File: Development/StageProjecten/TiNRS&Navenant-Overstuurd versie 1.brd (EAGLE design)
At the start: 180.7 x 105.1 mm, 377 parts, among them IC1 7809DT, IC10 LM13700M, IC11 TL074TSSOP14, IC2 TL074TSSOP14, IC3 TL074TSSOP14, IC4 TL074TSSOP14, IC5 LM13700M, IC6 TL074TSSOP14, IC7 TL074TSSOP14, IC8 TL074TSSOP14, IC9 TL074TSSOP14, J1 JACK, J10 JACK, J11 JACK, J12 JACK, J13 JACK, J14 JACK, J15 JACK, J16 JACK, J17 JACK, J18 JACK, J19 JACK, J2 POWERSHROUDED, J20 JACK, J21 JACK, J22 JACK, J23 JACK, J24 JACK, J25 JACK, J26 JACK, J27 JACK, J3 JACK, J4 JACK, J5 JACK, J6 JACK, J7 JACK, J8 JACK, J9 JACK, Q1 MMBT3906LT1SMD, Q3 MMBT3906LT1SMD, Q4 MMBT3906LT1SMD, T1 3906

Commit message: Pre-ARcomp gate update
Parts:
- removed ACID1:D3, ACID1:D4: 1N4148DO35-10, diode:DO35-10
- removed ACID1:JP1: GERMANIUMSELECTOR, pinhead@1:1X03
- removed ACID1:JP4: ACID+, pinhead:1X03
- removed ACID1:JP5: ACID-, pinhead:1X03
- removed ACID1:JP6: ACIDBIAS, pinhead:1X03
- removed CLIP1:JP1: CLIPBIAS, pinhead:1X03
- removed CLIP1:JP2: CLIP+, pinhead:1X03
- removed CLIP1:JP3: CLIP-, pinhead:1X03
- removed FUZZ1:T1, FUZZ1:T2: (no value), transistor-neu-to92@1:TO92-EBC
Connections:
- removed net ACID1:ACIDNE: ACID1:C24.1, ACID1:IC5.4, ACID1:JP5.2
- removed net ACID1:ACIDPL: ACID1:C25.1, ACID1:C7.+, ACID1:IC5.7, ACID1:JP4.2
- removed net ACID1:N$2: ACID1:D3.C, ACID1:D4.A, ACID1:JP1.3
- removed net ACID1:N$34: ACID1:C28.2, ACID1:JP1.2, ACID1:R22.P$3, ACID1:R24.P$3
- removed net ACID1:TO4.5V: ACID1:JP6.1, ACID1:R72.1
- removed net CLIP1:CLIPNE: CLIP1:C4.1, CLIP1:IC6.4, CLIP1:JP3.2
- removed net CLIP1:CLIPPL: CLIP1:C25.1, CLIP1:C7.+, CLIP1:IC6.7, CLIP1:JP2.2
- removed net CLIP1:N$41: CLIP1:JP1.1, CLIP1:R34.1
- new net ACID1:N$4: ACID1:C24.1, ACID1:IC5.4
- new net CLIP1:N$3: CLIP1:C4.1, CLIP1:IC6.4
- net -12V: no longer ACID1:JP5.3, CLIP1:JP3.3
- net 12V: no longer ACID1:JP4.3, CLIP1:JP2.3
- net 9V: now also ACID1:C25.1, ACID1:C7.+, ACID1:IC5.7, CLIP1:C25.1, CLIP1:C7.+, CLIP1:IC6.7; no longer ACID1:JP4.1, CLIP1:JP2.1, FUZZ1:T1.E
- net ACID1:ACIDVI: now also ACID1:R72.1; no longer ACID1:JP6.2
- net ACID1:N$3: now also ACID1:C28.2, ACID1:R22.P$3, ACID1:R24.P$3; no longer ACID1:JP1.1
- net CLIP1:CLIPVI: now also CLIP1:R34.1; no longer CLIP1:JP1.2
- net FUZZ1:N$53: no longer FUZZ1:T2.E
- net FUZZ1:N$54: no longer FUZZ1:T1.B
- net FUZZ1:N$55: no longer FUZZ1:T1.C, FUZZ1:T2.B
- net FUZZ1:N$59: no longer FUZZ1:T2.C
- net GND: no longer ACID1:D3.A, ACID1:D4.C, ACID1:JP5.1, CLIP1:JP3.1
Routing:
- net ACID1:N$34: track 97.1 -> 0.00 mm, vias 3 -> 0
- net ACID1:N$3: track 24.2 -> 83.4 mm, vias 0 -> 3
- net CLIP1:CLIPPL: track 41.6 -> 0.00 mm, vias 2 -> 0
- net ACID1:ACIDNE: track 22.8 -> 0.00 mm, vias 6 -> 0
- net CLIP1:CLIPVI: track 26.8 -> 4.63 mm, vias 1 -> 0
- net CLIP1:N$41: track 21.5 -> 0.00 mm
- net CLIP1:CLIPNE: track 17.1 -> 0.00 mm
- net 12V: track 504.7 -> 488.5 mm, vias 63 -> 61
- net ACID1:ACIDPL: track 15.7 -> 0.00 mm
- net 9V: track 213.2 -> 228.6 mm, vias 34 -> 32
- net -12V: track 474.4 -> 459.3 mm, vias 58 -> 54
- net FUZZ1:N$55: track 23.6 -> 14.7 mm
- net ACID1:N$2: track 7.62 -> 0.00 mm
- net ACID1:TO4.5V: track 6.11 -> 0.00 mm, vias 2 -> 0
- net FUZZ1:N$59: track 16.0 -> 12.0 mm
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
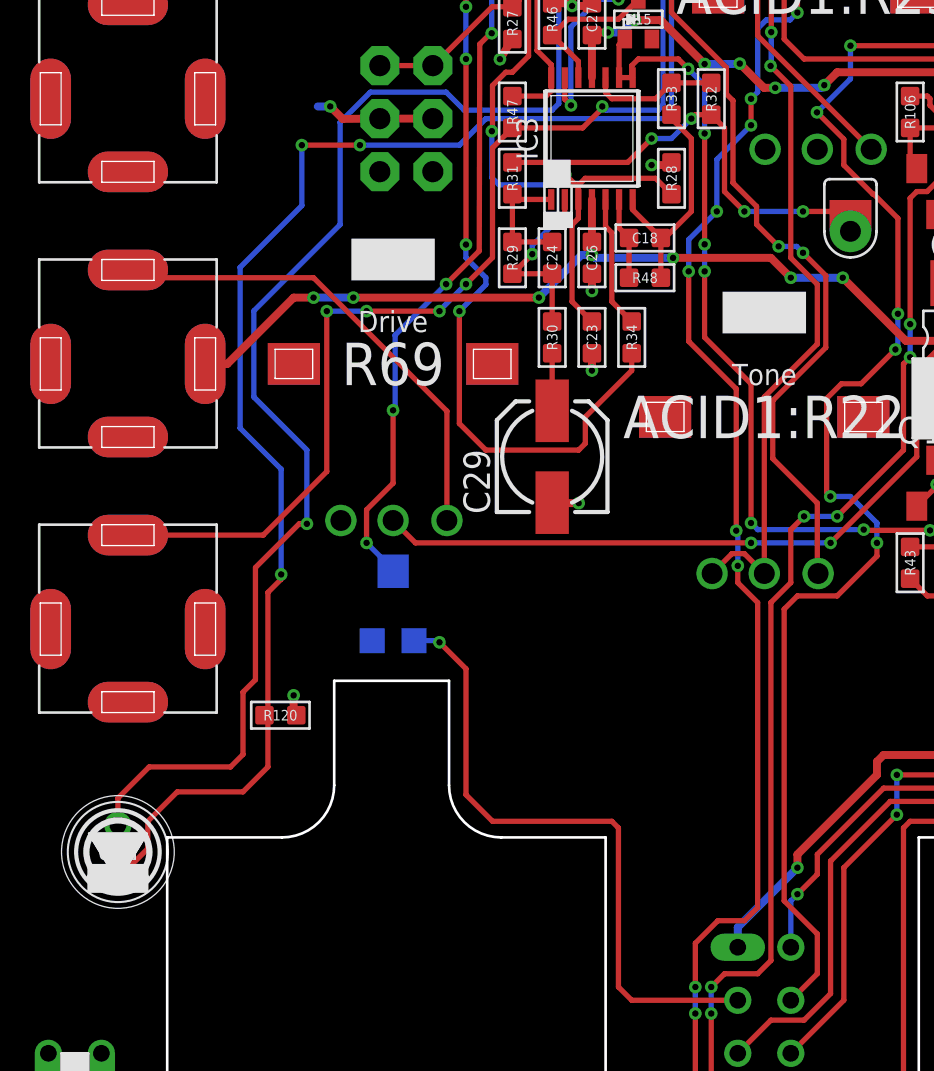
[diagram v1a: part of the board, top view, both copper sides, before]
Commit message: AR envelope gate
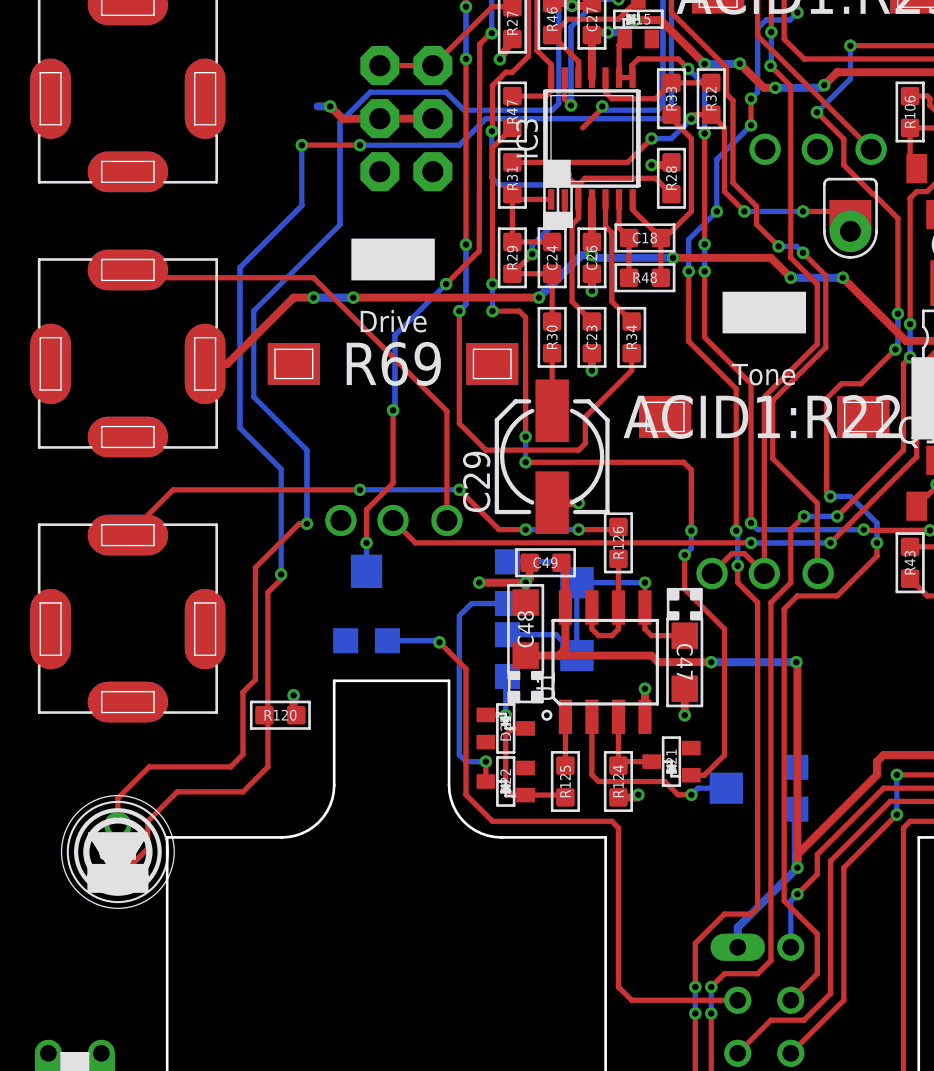
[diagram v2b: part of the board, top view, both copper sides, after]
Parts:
- added C47: 10uF, EurorackModularParts:CASE-A_3216
- added C48: 10u, EurorackModularParts:CASE-A_3216
- added C49: 100n, OPL:C0603
- added D21, D22, D23: BAS16W, FenixBase:SOT-323
- added R124: 100K, OPL:R0603
- added R125: 560 (33)R, OPL:R0603
- added R126: 1K, OPL:R0603
- added U$103, U$104, U$97: 50k, adafruit:TC33X
- added U1: LM358DR-1110010P1, OPL:SOIC8
- moved TR_IN_A 1.27 mm to (19.1, 31.8)
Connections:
- new net N$119: R125.1, U1.1
- new net N$120: D22.ANODE, D23.CATHODE, R125.2
- new net N$121: D22.CATHODE, U$103.1
- new net N$122: R126.2, U1.6, U1.7
- new net N$123: D23.ANODE, U$104.1
- new net N$124: C47.+, U$103.2, U$103.3, U$104.2, U$104.3, U1.5
- new net N$125: J24.TIP_B@1, J24.TIP_T@3, R126.1
- new net N$7: D21.CATHODE, R124.1, U1.3
- new net N$8: D21.ANODE, R47.1
- new net N$99: U$97.2, U1.2
- net 12V: now also C48.+, C49.2, U$97.3, U1.8
- net ENVELOPE_OUT: no longer J24.TIP_B@1, J24.TIP_T@3, R47.1
- net GND: now also C47.-, C48.-, C49.1, R124.2, U$97.1, U1.4
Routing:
- net N$8: track 0.00 -> 42.5 mm, vias 0 -> 6
- net ENVELOPE_OUT: track 246.2 -> 208.7 mm, vias 10 -> 6
- net 12V: track 488.5 -> 518.9 mm, vias 61 -> 63
- net N$125: track 0.00 -> 25.2 mm, vias 0 -> 4
- net N$124: track 0.00 -> 18.5 mm, vias 0 -> 1
- net N$121: track 0.00 -> 11.6 mm, vias 0 -> 1
- net N$99: track 0.00 -> 9.74 mm, vias 0 -> 1
- net GND: track 155.6 -> 163.4 mm, vias 107 -> 112
- net N$120: track 0.00 -> 6.66 mm
- net N$122: track 0.00 -> 5.93 mm
- net N$7: track 0.00 -> 4.01 mm
- net N$123: track 0.00 -> 2.85 mm, vias 0 -> 1
- net N$119: track 0.00 -> 2.34 mm
- net PEDAL_A: track 30.6 -> 31.9 mm
- net EURORACK_IN: track 51.2 -> 50.4 mm
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
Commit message: arboard los
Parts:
- removed C47: 10uF, EurorackModularParts:CASE-A_3216
- added C50: 22uF, OPL:C0603
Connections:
- net GND: now also C50.1; no longer C47.-
- net N$124: now also C50.2; no longer C47.+
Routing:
- net N$124: track 18.5 -> 19.1 mm, vias 1 -> 2
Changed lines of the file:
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@@
 <attribute name="VALUE" x="25.7175" y="32.385" size="1.27" layer="28" rot="MR180"/>
 </element>
-<element name="C47" library="EurorackModularParts" package="CASE-A_3216" value="10uF" x="34.29" y="28.8925" smashed="yes" rot="R270">
-<attribute name="NAME" x="34.29" y="28.8925" size="0.762" layer="25" ratio="10" rot="SR270" align="center"/>
-<attribute name="VALUE" x="32.798" y="30.4925" size="0.635" layer="27" ratio="10" rot="R270"/>
-</element>
 <element name="R126" library="OPL" package="R0603" value="1K" x="31.115" y="34.6075" smashed="yes" rot="R270">
 <attribute name="NAME" x="31.115" y="34.6075" size="0.508" layer="25" ratio="11" rot="R270" align="center"/>
@@
 <attribute name="VALUE" x="27.6225" y="32.7025" size="0.508" layer="27" ratio="10" align="top-center"/>
 </element>
+<element name="C50" library="OPL" package="C0603" value="22uF" x="23.495" y="31.115" smashed="yes">
+<attribute name="NAME" x="23.495" y="31.115" size="0.508" layer="25" ratio="11" align="center"/>
+<attribute name="VALUE" x="23.495" y="30.1625" size="0.508" layer="27" ratio="10" align="top-center"/>
+</element>
 </elements>
 <signals>
@@
 <contactref element="R124" pad="2"/>
 <contactref element="U$97" pad="1"/>
-<contactref element="C47" pad="-"/>
 <contactref element="C48" pad="-"/>
 <contactref element="C49" pad="1"/>
@@
 <wire x1="26.8605" y1="32.893" x2="26.67" y2="32.7025" width="0.381" layer="1"/>
 <wire x1="26.67" y1="31.75" x2="26.67" y2="32.7025" width="0.381" layer="1"/>
-<wire x1="34.29" y1="27.6225" x2="34.29" y2="26.3525" width="0.381" layer="1"/>
-<via x="34.29" y="26.3525" extent="1-16" drill="0.3048"/>
 <wire x1="32.385" y1="26.2763" x2="32.385" y2="27.6225" width="0.381" layer="1"/>
 <via x="32.385" y="27.6225" extent="1-16" drill="0.3048"/>
@@
 <wire x1="26.67" y1="32.7025" x2="24.4475" y2="32.7025" width="0.381" layer="1"/>
 <via x="24.4475" y="32.7025" extent="1-16" drill="0.3048"/>
+<contactref element="C50" pad="1"/>
+<wire x1="22.733" y1="31.115" x2="21.9075" y2="31.115" width="0.381" layer="1"/>
+<via x="21.9075" y="31.115" extent="1-16" drill="0.3048"/>
 </signal>
 <signal name="OUTPUT_A">
@@
 <contactref element="U$103" pad="2"/>
 <contactref element="U$103" pad="3"/>
-<contactref element="C47" pad="+"/>
 <contactref element="U1" pad="5"/>
 <wire x1="32.385" y1="31.5087" x2="32.385" y2="30.48" width="0.254" layer="1"/>
 <wire x1="32.385" y1="30.48" x2="32.7025" y2="30.1625" width="0.254" layer="1"/>
-<wire x1="32.7025" y1="30.1625" x2="34.29" y2="30.1625" width="0.254" layer="1"/>
 <wire x1="25.7975" y1="30.21" x2="28.1225" y2="30.21" width="0.254" layer="16"/>
 <wire x1="28.1225" y1="30.21" x2="29.1225" y2="29.21" width="0.254" layer="16"/>
@@
 <via x="32.385" y="32.7025" extent="1-16" drill="0.3048"/>
 <wire x1="32.385" y1="32.7025" x2="32.385" y2="31.5087" width="0.254" layer="1"/>
+<contactref element="C50" pad="2"/>
+<wire x1="24.257" y1="31.115" x2="24.765" y2="30.607" width="0.254" layer="1"/>
+<wire x1="24.765" y1="30.607" x2="24.765" y2="30.1625" width="0.254" layer="1"/>
+<via x="24.765" y="30.1625" extent="1-16" drill="0.3048"/>
+<wire x1="24.765" y1="30.1625" x2="24.8125" y2="30.21" width="0.254" layer="16"/>
+<wire x1="24.8125" y1="30.21" x2="25.7975" y2="30.21" width="0.254" layer="16"/>
 </signal>
 <signal name="N$123">

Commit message: Summing mixer - envelope_out link
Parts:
- added R127: 100K, OPL:R0603
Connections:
- removed net N$125: J24.TIP_B@1, J24.TIP_T@3, R126.1
- net ENVELOPE_OUT: now also J24.TIP_B@1, J24.TIP_T@3, R126.1
- net GND: now also IC3.10
- net MIX_OUT: now also R127.1; no longer IC3.9
- net VCA_SIG_IN: now also IC3.9, R127.2; no longer IC3.10
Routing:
- net N$125: track 25.2 -> 0.00 mm, vias 4 -> 0
- net ENVELOPE_OUT: track 208.7 -> 233.9 mm, vias 6 -> 10
- net MIX_OUT: track 42.5 -> 40.3 mm
- net VCA_SIG_IN: track 6.22 -> 5.51 mm
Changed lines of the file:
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@@
 <?xml version="1.0" encoding="utf-8"?>
 <!DOCTYPE eagle SYSTEM "eagle.dtd">
-<eagle version="9.5.2">
+<eagle version="9.5.1">
 <drawing>
 <settings>
@@
 <attribute name="VALUE" x="23.495" y="30.1625" size="0.508" layer="27" ratio="10" align="top-center"/>
 </element>
+<element name="R127" library="OPL" package="R0603" value="100K" x="-0.3175" y="-11.7475" smashed="yes">
+<attribute name="NAME" x="-0.3175" y="-11.7475" size="0.508" layer="25" ratio="11" align="center"/>
+<attribute name="VALUE" x="-1.7145" y="-13.065" size="0.508" layer="27" ratio="10"/>
+</element>
 </elements>
 <signals>
@@
 <wire x1="22.733" y1="31.115" x2="21.9075" y2="31.115" width="0.381" layer="1"/>
 <via x="21.9075" y="31.115" extent="1-16" drill="0.3048"/>
+<contactref element="IC3" pad="10"/>
+<wire x1="29.845" y1="60.452" x2="30.495" y2="56.8928" width="0" layer="19" extent="1-1"/>
 </signal>
 <signal name="OUTPUT_A">
@@
 <contactref element="R33" pad="1"/>
 <contactref element="R32" pad="1"/>
-<contactref element="IC3" pad="10"/>
 <wire x1="33.655" y1="56.642" x2="35.56" y2="56.642" width="0.254" layer="1"/>
-<wire x1="30.495" y1="56.8928" x2="30.495" y2="56.1825" width="0.254" layer="1"/>
 <wire x1="30.495" y1="56.1825" x2="30.7975" y2="55.88" width="0.254" layer="1"/>
 <wire x1="30.7975" y1="55.88" x2="32.893" y2="55.88" width="0.254" layer="1"/>
 <wire x1="32.893" y1="55.88" x2="33.655" y2="56.642" width="0.254" layer="1"/>
+<contactref element="IC3" pad="9"/>
+<contactref element="R127" pad="2"/>
+<wire x1="31.145" y1="56.8928" x2="30.495" y2="56.1825" width="0" layer="19" extent="1-1"/>
+<wire x1="0.4445" y1="-11.7475" x2="30.495" y2="56.1825" width="0" layer="19" extent="1-1"/>
 </signal>
 <signal name="N$54">
@@
 <signal name="MIX_OUT">
 <contactref element="R35" pad="1"/>
-<contactref element="IC3" pad="9"/>
 <contactref element="IC3" pad="8"/>
 <contactref element="D15" pad="ANODE"/>
-<wire x1="31.145" y1="56.8928" x2="31.145" y2="58.4675" width="0.254" layer="1"/>
 <wire x1="31.145" y1="58.4675" x2="31.4175" y2="58.74" width="0.254" layer="1"/>
-<wire x1="31.145" y1="56.8928" x2="31.795" y2="56.8928" width="0.254" layer="1"/>
 <wire x1="48.895" y1="37.973" x2="48.895" y2="36.9697" width="0.254" layer="1"/>
 <wire x1="48.895" y1="36.9697" x2="48.7553" y2="36.83" width="0.254" layer="1"/>
@@
 <wire x1="37.465" y1="42.2275" x2="35.2425" y2="44.45" width="0.254" layer="1"/>
 <wire x1="33.98248125" y1="57.785" x2="32.0675" y2="57.785" width="0.254" layer="1"/>
+<contactref element="R127" pad="1"/>
+<wire x1="31.795" y1="56.8928" x2="31.145" y2="58.4675" width="0" layer="19" extent="1-1"/>
+<wire x1="-1.0795" y1="-11.7475" x2="37.465" y2="35.56" width="0" layer="19" extent="1-1"/>
 </signal>
 <signal name="N$60">
@@
 <wire x1="168.8" y1="81.28" x2="168.8592" y2="81.3392" width="0.254" layer="1"/>
 <wire x1="168.8592" y1="81.3392" x2="168.8592" y2="88.3158" width="0.254" layer="1"/>
+<contactref element="J24" pad="TIP_B@1" route="any" routetag="G$1.TIP"/>
+<contactref element="J24" pad="TIP_T@3" route="any" routetag="G$1.TIP"/>
+<contactref element="R126" pad="1"/>
+<wire x1="7.62" y1="34.98" x2="9.7875" y2="37.1475" width="0.254" layer="1"/>
+<wire x1="9.7875" y1="37.1475" x2="18.7325" y2="37.1475" width="0.254" layer="1"/>
+<via x="18.7325" y="37.1475" extent="1-16" drill="0.3048"/>
+<wire x1="18.7325" y1="37.1475" x2="23.495" y2="37.1475" width="0.254" layer="16"/>
+<via x="23.495" y="37.1475" extent="1-16" drill="0.3048"/>
+<wire x1="23.495" y1="37.1475" x2="25.4" y2="35.2425" width="0.254" layer="1"/>
+<wire x1="25.4" y1="35.2425" x2="26.67" y2="35.2425" width="0.254" layer="1"/>
+<via x="26.67" y="35.2425" extent="1-16" drill="0.3048"/>
+<wire x1="26.67" y1="35.2425" x2="29.21" y2="35.2425" width="0.254" layer="16"/>
+<via x="29.21" y="35.2425" extent="1-16" drill="0.3048"/>
+<wire x1="29.21" y1="35.2425" x2="30.988" y2="35.2425" width="0.254" layer="1"/>
+<wire x1="30.988" y1="35.2425" x2="31.115" y2="35.3695" width="0.254" layer="1"/>
+<wire x1="29.4005" y1="54.483" x2="23.495" y2="37.1475" width="0" layer="19" extent="1-1"/>
 </signal>
 <signal name="N$62">
@@
 <wire x1="31.115" y1="30.48" x2="31.115" y2="31.5087" width="0.254" layer="1"/>
 </signal>
-<signal name="N$125">
-<contactref element="J24" pad="TIP_B@1" route="any" routetag="G$1.TIP"/>
-<contactref element="J24" pad="TIP_T@3" route="any" routetag="G$1.TIP"/>
-<contactref element="R126" pad="1"/>
-<wire x1="7.62" y1="34.98" x2="9.7875" y2="37.1475" width="0.254" layer="1"/>
-<wire x1="9.7875" y1="37.1475" x2="18.7325" y2="37.1475" width="0.254" layer="1"/>
-<via x="18.7325" y="37.1475" extent="1-16" drill="0.3048"/>
-<wire x1="18.7325" y1="37.1475" x2="23.495" y2="37.1475" width="0.254" layer="16"/>
-<via x="23.495" y="37.1475" extent="1-16" drill="0.3048"/>
-<wire x1="23.495" y1="37.1475" x2="25.4" y2="35.2425" width="0.254" layer="1"/>
-<wire x1="25.4" y1="35.2425" x2="26.67" y2="35.2425" width="0.254" layer="1"/>
-<via x="26.67" y="35.2425" extent="1-16" drill="0.3048"/>
-<wire x1="26.67" y1="35.2425" x2="29.21" y2="35.2425" width="0.254" layer="16"/>
-<via x="29.21" y="35.2425" extent="1-16" drill="0.3048"/>
-<wire x1="29.21" y1="35.2425" x2="30.988" y2="35.2425" width="0.254" layer="1"/>
-<wire x1="30.988" y1="35.2425" x2="31.115" y2="35.3695" width="0.254" layer="1"/>
-</signal>
 </signals>

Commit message: more wrong trace cleanup
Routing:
- net ENVELOPE_OUT: track 233.9 -> 229.4 mm, vias 10 -> 9
- net VCA_SIG_IN: track 5.51 -> 1.91 mm
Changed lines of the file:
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@@
 <contactref element="R32" pad="1"/>
 <wire x1="33.655" y1="56.642" x2="35.56" y2="56.642" width="0.254" layer="1"/>
-<wire x1="30.495" y1="56.1825" x2="30.7975" y2="55.88" width="0.254" layer="1"/>
-<wire x1="30.7975" y1="55.88" x2="32.893" y2="55.88" width="0.254" layer="1"/>
-<wire x1="32.893" y1="55.88" x2="33.655" y2="56.642" width="0.254" layer="1"/>
 <contactref element="IC3" pad="9"/>
 <contactref element="R127" pad="2"/>
-<wire x1="31.145" y1="56.8928" x2="30.495" y2="56.1825" width="0" layer="19" extent="1-1"/>
-<wire x1="0.4445" y1="-11.7475" x2="30.495" y2="56.1825" width="0" layer="19" extent="1-1"/>
+<wire x1="31.145" y1="56.8928" x2="33.655" y2="56.642" width="0" layer="19" extent="1-1"/>
+<wire x1="0.4445" y1="-11.7475" x2="31.145" y2="56.8928" width="0" layer="19" extent="1-1"/>
 </signal>
 <signal name="N$54">
@@
 <wire x1="30.7086" y1="75.0791625" x2="31.5802" y2="74.2075625" width="0.254" layer="16"/>
 <wire x1="31.5802" y1="73.1836125" x2="33.2486" y2="71.5152125" width="0.254" layer="16"/>
-<wire x1="33.2486" y1="55.5625" x2="33.02" y2="55.3339" width="0.254" layer="16"/>
-<wire x1="33.02" y1="55.3339" x2="30.5174125" y2="55.3339" width="0.254" layer="16"/>
-<wire x1="30.5174125" y1="55.3339" x2="30.3396125" y2="55.5117" width="0.254" layer="16"/>
-<via x="30.3396125" y="55.5117" extent="1-16" drill="0.3048"/>
-<wire x1="30.3396125" y1="55.5117" x2="30.3396125" y2="55.4221125" width="0.254" layer="1"/>
 <wire x1="36.5125" y1="99.8347" x2="36.5125" y2="98.1075" width="0.254" layer="16"/>
 <wire x1="36.5125" y1="98.1075" x2="34.5186" y2="96.1136" width="0.254" layer="16"/>
@@
 <wire x1="30.7086" y1="83.9691625" x2="30.7086" y2="75.0791625" width="0.254" layer="16"/>
 <wire x1="33.2486" y1="71.5152125" x2="33.2486" y2="55.5625" width="0.254" layer="16"/>
-<wire x1="30.3396125" y1="55.4221125" x2="29.4005" y2="54.483" width="0.254" layer="1"/>
 <wire x1="157.48" y1="90.4875" x2="166.6875" y2="90.4875" width="0.254" layer="1"/>
 <wire x1="166.6875" y1="90.4875" x2="168.8592" y2="88.3158" width="0.254" layer="1"/>
@@
 <wire x1="29.21" y1="35.2425" x2="30.988" y2="35.2425" width="0.254" layer="1"/>
 <wire x1="30.988" y1="35.2425" x2="31.115" y2="35.3695" width="0.254" layer="1"/>
-<wire x1="29.4005" y1="54.483" x2="23.495" y2="37.1475" width="0" layer="19" extent="1-1"/>
+<wire x1="33.2486" y1="55.5625" x2="31.115" y2="35.3695" width="0" layer="19" extent="1-16"/>
 </signal>
 <signal name="N$62">

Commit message: Update Overstuur Board
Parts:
- moved R127 65.7 mm to (33.7, 44.5), turned to 90 degrees
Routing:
- net ENVELOPE_OUT: track 229.4 -> 257.6 mm, vias 9 -> 16
- net VCA_SIG_IN: track 1.91 -> 20.3 mm, vias 0 -> 6
- net FUZZ1:N$59: track 12.0 -> 2.21 mm
- net MIX_OUT: track 40.3 -> 46.0 mm, vias 8 -> 10
- net ACID1:ACIDVI: track 15.3 -> 11.1 mm
- net 12V: track 518.9 -> 516.1 mm
- net FUZZ1:N$55: track 14.7 -> 13.1 mm
- net N$124: track 19.1 -> 17.6 mm
- net GND: track 162.9 -> 164.2 mm, vias 112 -> 113
- net OUTPUT_A: vias 20 -> 18
